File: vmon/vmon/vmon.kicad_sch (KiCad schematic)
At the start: 59 parts, among them J3 Conn_01x02_Pin, J4 Conn_01x04_Pin, Q1 BC847, Q2 SI2300DS, U5 PC817, U6 PC817, U7 PC817

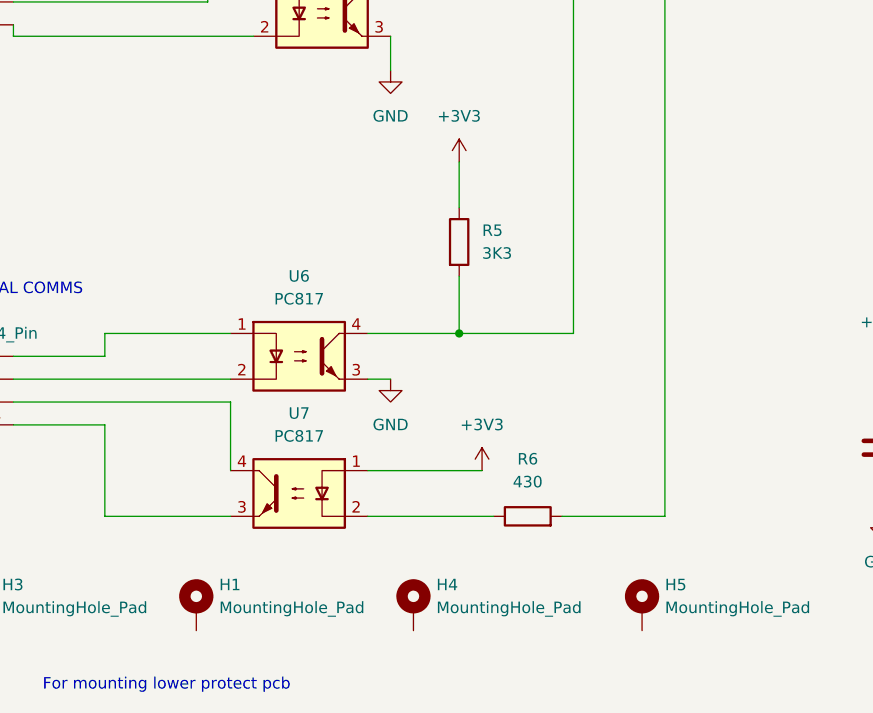
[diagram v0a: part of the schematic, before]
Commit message: add a top level schematic
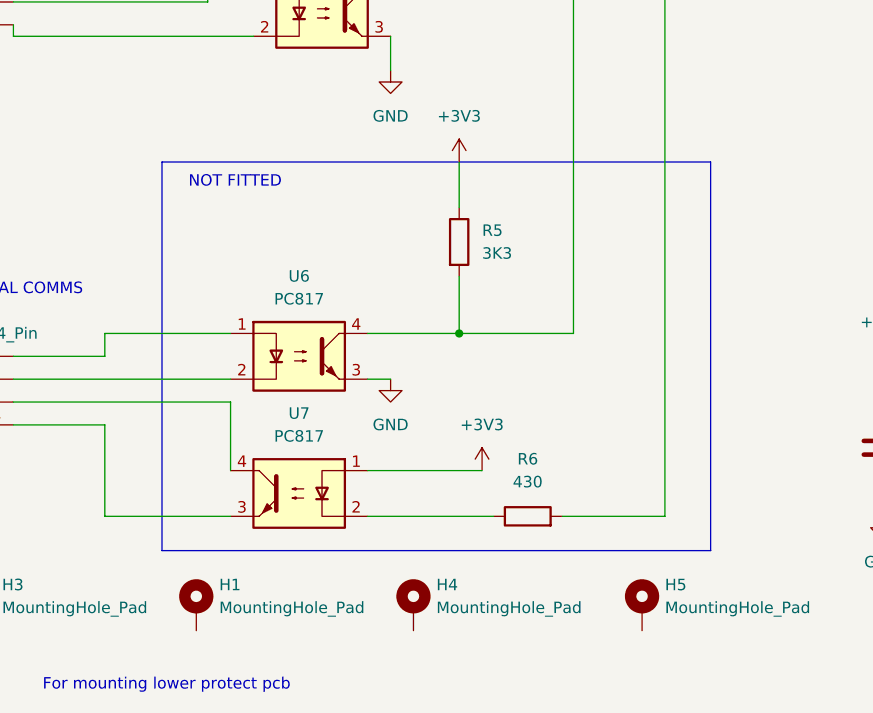
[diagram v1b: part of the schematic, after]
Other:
- note added: "NOT FITTED"
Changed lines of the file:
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@@
 (kicad_sch
-	(version 20231120)
+	(version 20250114)
 	(generator "eeschema")
-	(generator_version "8.0")
+	(generator_version "9.0")
 	(paper "A4")
+	(rectangle
+		(start 44.45 134.62)
+		(end 105.41 177.8)
+		(stroke
+			(width 0)
+			(type default)
+		)
+		(fill
+			(type none)
+		)
+	)
+	(text "VMON"
+		(exclude_from_sim no)
+		(at 228.092 190.246 0)
+		(effects
+			(font
+				(size 1.27 1.27)
+			)
+		)
+	)
+	(text "25 Feb 2025"
+		(exclude_from_sim no)
+		(at 225.298 193.548 0)
+		(effects
+			(font
+				(size 1.27 1.27)
+			)
+		)
+	)
+	(text "BATTERY TEMPERATURE\nNEAR B+ CONN + THERMALS"
+		(exclude_from_sim no)
+		(at 71.374 15.494 0)
+		(effects
+			(font
+				(size 1.27 1.27)
+			)
+		)
+	)
+	(text "For mounting lower protect pcb\n"
+		(exclude_from_sim no)
+		(at 44.958 192.786 0)
+		(effects
+			(font
+				(size 1.27 1.27)
+			)
+		)
+	)
+	(text "B- flying lead"
+		(exclude_from_sim no)
+		(at 20.828 67.818 0)
+		(effects
+			(font
+				(size 1.27 1.27)
+			)
+		)
+	)
+	(text "MASTER SERIAL COMMS"
+		(exclude_from_sim no)
+		(at 25.146 148.844 0)
+		(effects
+			(font
+				(size 1.27 1.27)
+			)
+		)
+	)
+	(text "NOT FITTED"
+		(exclude_from_sim no)
+		(at 52.578 136.906 0)
+		(effects
+			(font
+				(size 1.27 1.27)
+			)
+		)
+	)
+	(text "PASSIVE BALANCE RESISTORS  350mA\n"
+		(exclude_from_sim no)
+		(at 203.2 33.782 0)
+		(effects
+			(font
+				(size 1.27 1.27)
+			)
+		)
+	)
+	(text "ENABLE IN"
+		(exclude_from_sim no)
+		(at 21.336 124.206 0)
+		(effects
+			(font
+				(size 1.27 1.27)
+			)
+		)
+	)
+	(text "BATT B+ POST BOLTHOLE\nBIG THERMAL PAD\n"
+		(exclude_from_sim no)
+		(at 24.13 46.99 0)
+		(effects
+			(font
+				(size 1.27 1.27)
+			)
+		)
+	)
+	(text "modules all have caps"
+		(exclude_from_sim no)
+		(at 136.398 186.944 0)
+		(effects
+			(font
+				(size 1.27 1.27)
+			)
+		)
+	)
+	(text "Resistor Temperature"
+		(exclude_from_sim no)
+		(at 262.382 52.324 0)
+		(effects
+			(font
+				(size 1.27 1.27)
+			)
+		)
+	)
+	(text "1"
+		(exclude_from_sim no)
+		(at 274.574 193.548 0)
+		(effects
+			(font
+				(size 1.27 1.27)
+			)
+		)
+	)
 	(junction
 		(at 214.63 68.58)
@@
 		)
 	)
-	(text "VMON"
-		(exclude_from_sim no)
-		(at 228.092 190.246 0)
-		(effects
-			(font
-				(size 1.27 1.27)
-			)
-		)
-	)
-	(text "25 Feb 2025"
-		(exclude_from_sim no)
-		(at 225.298 193.548 0)
-		(effects
-			(font
-				(size 1.27 1.27)
-			)
-		)
-	)
-	(text "BATTERY TEMPERATURE\nNEAR B+ CONN + THERMALS"
-		(exclude_from_sim no)
-		(at 71.374 15.494 0)
-		(effects
-			(font
-				(size 1.27 1.27)
-			)
-		)
-	)
-	(text "For mounting lower protect pcb\n"
-		(exclude_from_sim no)
-		(at 44.958 192.786 0)
-		(effects
-			(font
-				(size 1.27 1.27)
-			)
-		)
-	)
-	(text "B- flying lead"
-		(exclude_from_sim no)
-		(at 20.828 67.818 0)
-		(effects
-			(font
-				(size 1.27 1.27)
-			)
-		)
-	)
-	(text "MASTER SERIAL COMMS"
-		(exclude_from_sim no)
-		(at 25.146 148.844 0)
-		(effects
-			(font
-				(size 1.27 1.27)
-			)
-		)
-	)
-	(text "PASSIVE BALANCE RESISTORS  350mA\n"
-		(exclude_from_sim no)
-		(at 203.2 33.782 0)
-		(effects
-			(font
-				(size 1.27 1.27)
-			)
-		)
-	)
-	(text "ENABLE IN"
-		(exclude_from_sim no)
-		(at 21.336 124.206 0)
-		(effects
-			(font
-				(size 1.27 1.27)
-			)
-		)
-	)
-	(text "BATT B+ POST BOLTHOLE\nBIG THERMAL PAD\n"
-		(exclude_from_sim no)
-		(at 24.13 46.99 0)
-		(effects
-			(font
-				(size 1.27 1.27)
-			)
-		)
-	)
-	(text "modules all have caps"
-		(exclude_from_sim no)
-		(at 136.398 186.944 0)
-		(effects
-			(font
-				(size 1.27 1.27)
-			)
-		)
-	)
-	(text "Resistor Temperature"
-		(exclude_from_sim no)
-		(at 262.382 52.324 0)
-		(effects
-			(font
-				(size 1.27 1.27)
-			)
-		)
-	)
-	(text "1"
-		(exclude_from_sim no)
-		(at 274.574 193.548 0)
-		(effects
-			(font
-				(size 1.27 1.27)
-			)
-		)
-	)
 	(label "MISO"
 		(at 124.46 111.76 0)
@@
 		)
 	)
+	(embedded_fonts no)
 )
